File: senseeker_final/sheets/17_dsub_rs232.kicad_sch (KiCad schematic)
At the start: 8 parts, among them P1 Header-Male-2.54_2x2, U8 MAX3232CDBR

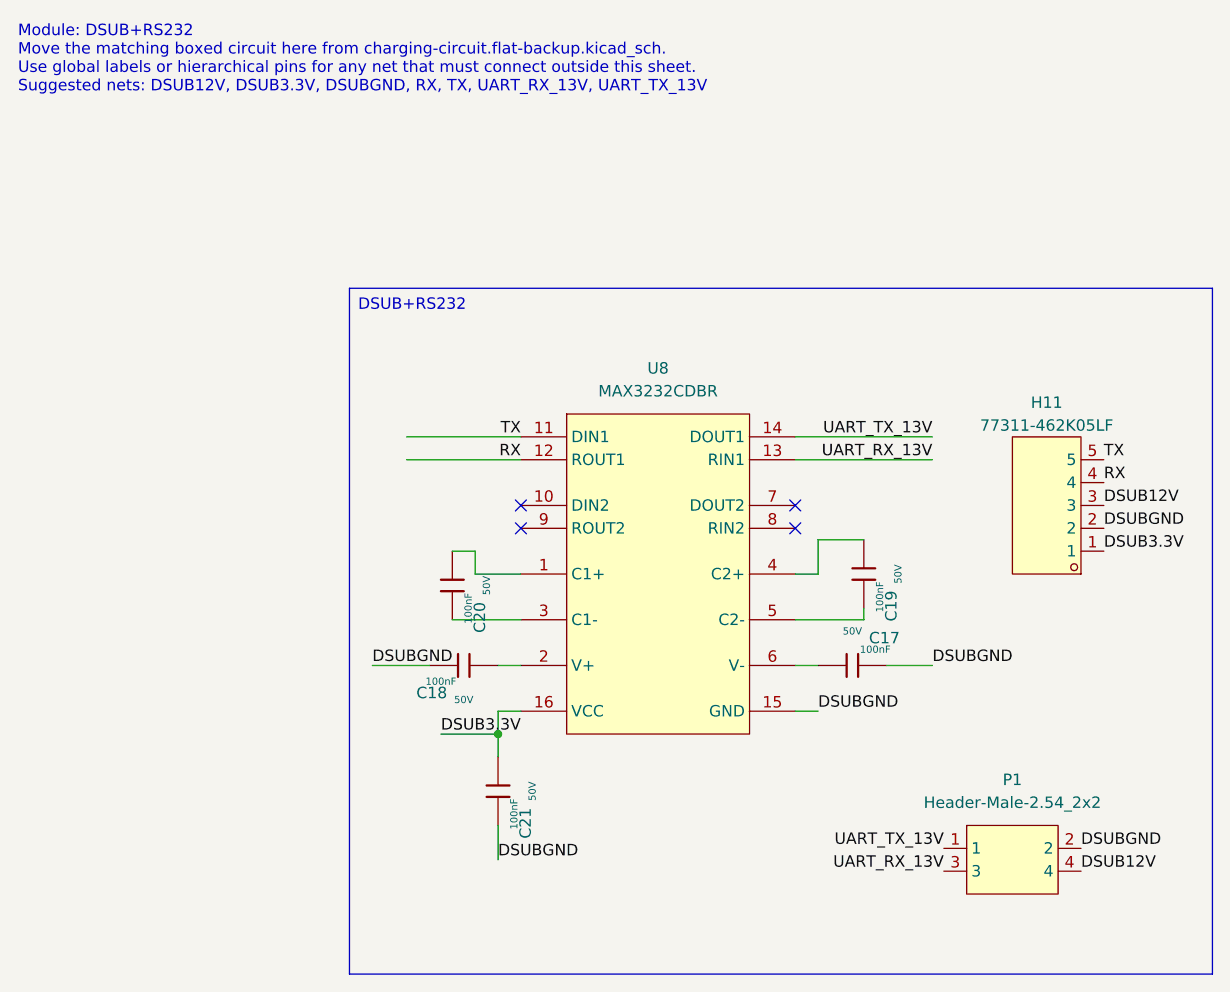
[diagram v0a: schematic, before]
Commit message: formatting changes for LM2596, now ready to branch of off and make our seperate PCB and then compare
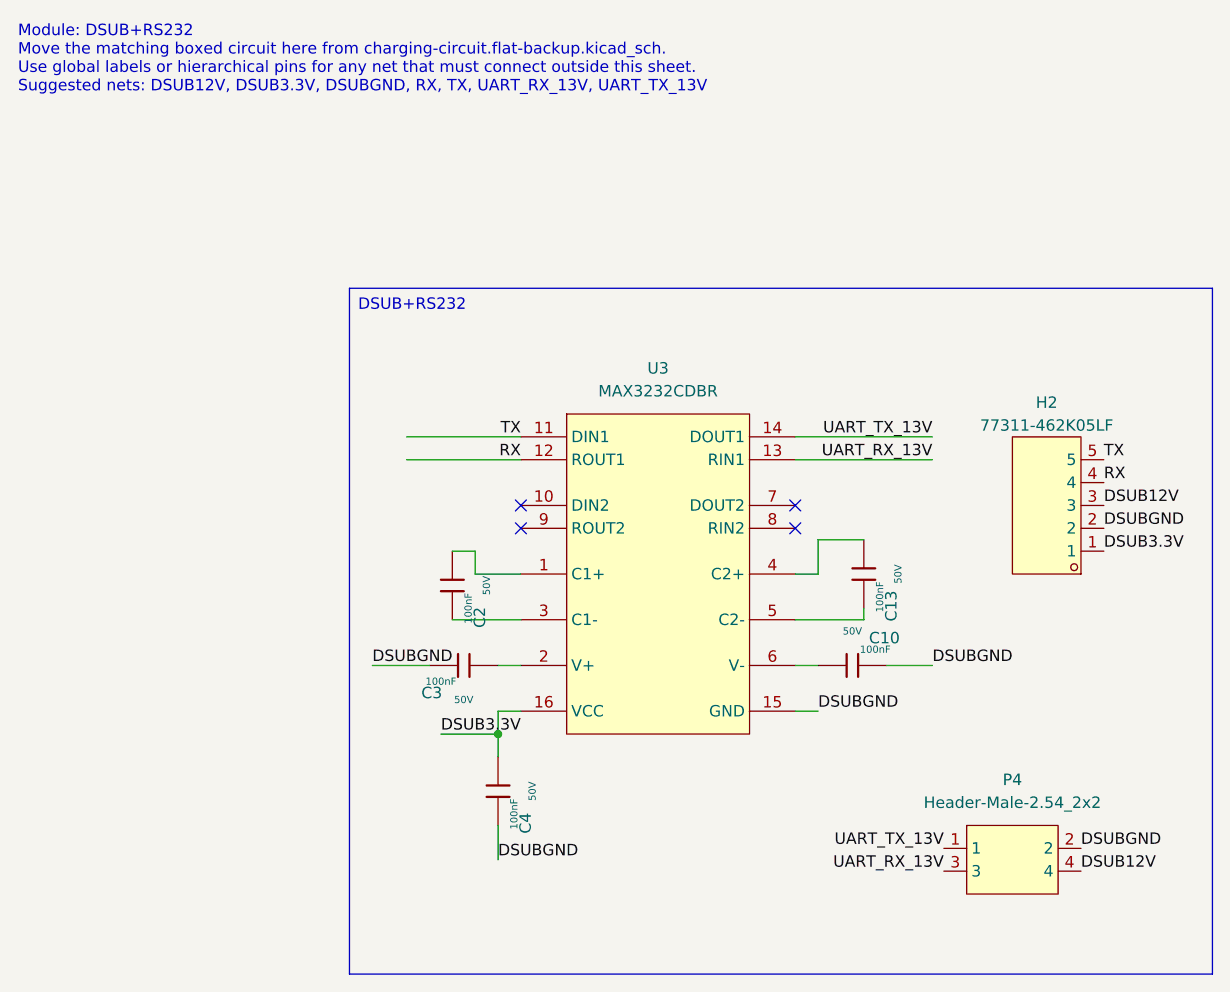
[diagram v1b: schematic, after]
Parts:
- renumbered C17 to C10, C19 to C13, C20 to C2, C18 to C3, C21 to C4, H11 to H2, P1 to P4, U8 to U3
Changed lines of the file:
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@@
 		(on_board yes)
 		(dnp no)
-		(property "Reference" "C17"
+		(property "Reference" "C10"
 			(at 121.666 89.662 90)
 			(effects
@@
 			(project "senseeker_final"
 				(path "/529bc8a5-ffae-43ac-972d-caccc3afab85/cebc8927-3eb9-4228-bd64-eb01f991daf3"
-					(reference "C17")
+					(reference "C10")
 					(unit 1)
 				)
@@
 		(on_board yes)
 		(dnp no)
-		(property "Reference" "C19"
+		(property "Reference" "C13"
 			(at 122.428 86.106 90)
 			(effects
@@
 			(project "senseeker_final"
 				(path "/529bc8a5-ffae-43ac-972d-caccc3afab85/cebc8927-3eb9-4228-bd64-eb01f991daf3"
-					(reference "C19")
+					(reference "C13")
 					(unit 1)
 				)
@@
 		(dnp no)
 		(fields_autoplaced yes)
-		(property "Reference" "H11"
+		(property "Reference" "H2"
 			(at 139.7 63.5 0)
 			(effects
@@
 			(project "senseeker_final"
 				(path "/529bc8a5-ffae-43ac-972d-caccc3afab85/cebc8927-3eb9-4228-bd64-eb01f991daf3"
-					(reference "H11")
+					(reference "H2")
 					(unit 1)
 				)
@@
 		(on_board yes)
 		(dnp no)
-		(property "Reference" "C20"
+		(property "Reference" "C2"
 			(at 76.708 87.376 90)
 			(effects
@@
 			(project "senseeker_final"
 				(path "/529bc8a5-ffae-43ac-972d-caccc3afab85/cebc8927-3eb9-4228-bd64-eb01f991daf3"
-					(reference "C20")
+					(reference "C2")
 					(unit 1)
 				)
@@
 		(on_board yes)
 		(dnp no)
-		(property "Reference" "C18"
+		(property "Reference" "C3"
 			(at 71.374 95.758 90)
 			(effects
@@
 			(project "senseeker_final"
 				(path "/529bc8a5-ffae-43ac-972d-caccc3afab85/cebc8927-3eb9-4228-bd64-eb01f991daf3"
-					(reference "C18")
+					(reference "C3")
 					(unit 1)
 				)
@@
 		(dnp no)
 		(fields_autoplaced yes)
-		(property "Reference" "U8"
+		(property "Reference" "U3"
 			(at 96.52 59.69 0)
 			(effects
@@
 			(project "senseeker_final"
 				(path "/529bc8a5-ffae-43ac-972d-caccc3afab85/cebc8927-3eb9-4228-bd64-eb01f991daf3"
-					(reference "U8")
+					(reference "U3")
 					(unit 1)
 				)
@@
 		(on_board yes)
 		(dnp no)
-		(property "Reference" "C21"
+		(property "Reference" "C4"
 			(at 81.788 110.236 90)
 			(effects
@@
 			(project "senseeker_final"
 				(path "/529bc8a5-ffae-43ac-972d-caccc3afab85/cebc8927-3eb9-4228-bd64-eb01f991daf3"
-					(reference "C21")
+					(reference "C4")
 					(unit 1)
 				)
@@
 		(dnp no)
 		(fields_autoplaced yes)
-		(property "Reference" "P1"
+		(property "Reference" "P4"
 			(at 135.89 105.41 0)
 			(effects
@@
 			(project "senseeker_final"
 				(path "/529bc8a5-ffae-43ac-972d-caccc3afab85/cebc8927-3eb9-4228-bd64-eb01f991daf3"
-					(reference "P1")
-					(unit 1)
-				)
+					(reference "P4")
+					(unit 1)
+				)
